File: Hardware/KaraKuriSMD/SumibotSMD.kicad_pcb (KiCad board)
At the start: 2 copper layers, 66 x 51.7 mm, 102 parts, among them J1 USB_B_Micro, M1 Left, M2 Right, Q1 DMG2301L, Q2 DMG2301L, Q3 DMG2301L, Q4 MBT3904DW1, Q5 DMG3406L, SW1 SW_SPDT, SW2 Reset, SW3 Boot, SW4 A, SW5 B, SW6 C, U1 MCP73831-3-OT, U2 AP2112K-3.3, U3 ESP32-WROOM-32, U4 MPU-9250, U5 LP2985-3.3, U6 DRV8870DDA, U7 CH340C, U8 DRV8870DDA

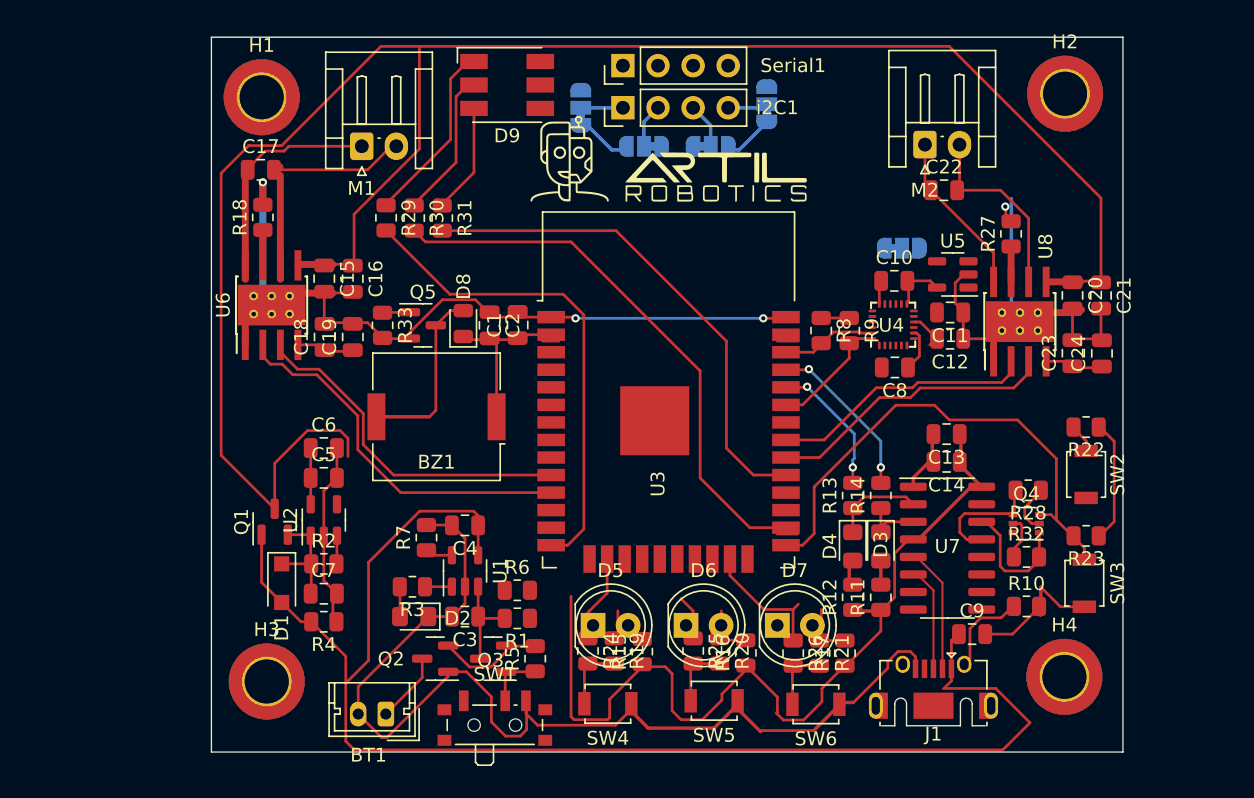
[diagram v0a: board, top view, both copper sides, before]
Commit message: Aplique  jerarquía para trabajar en colaborativo
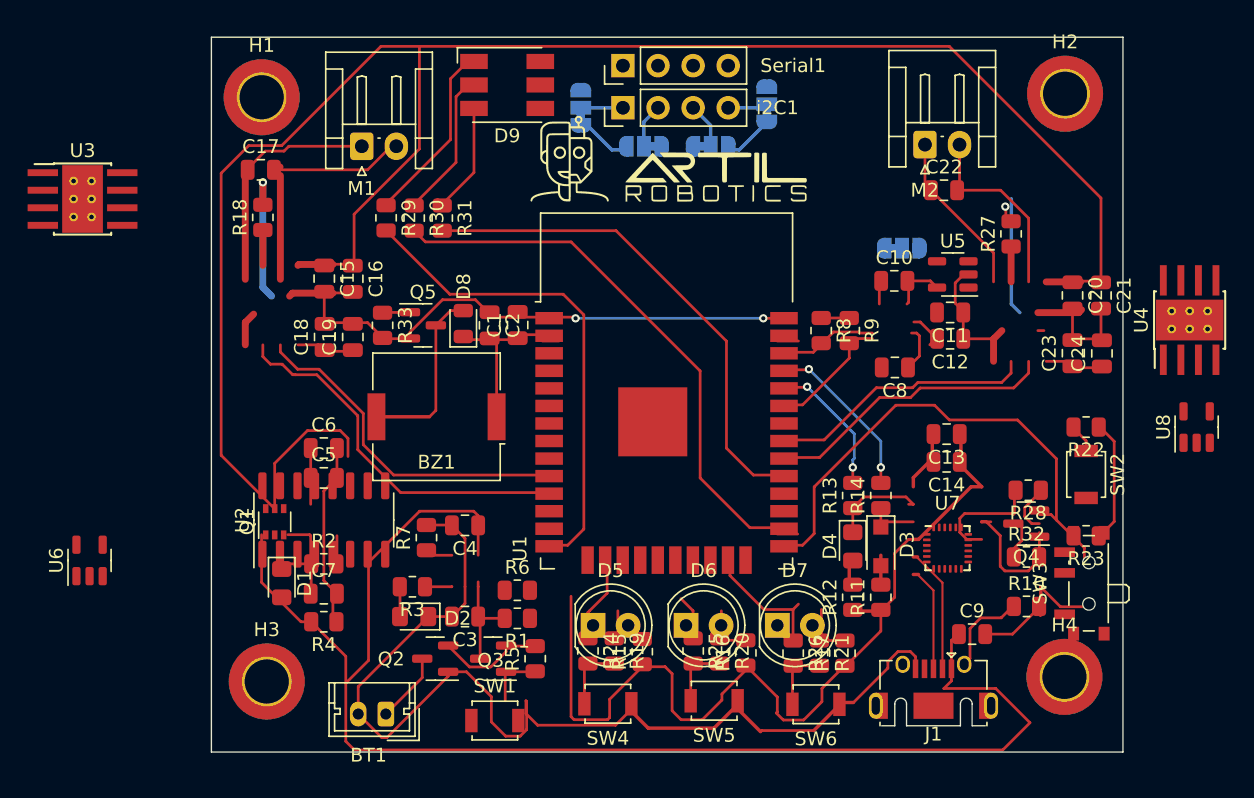
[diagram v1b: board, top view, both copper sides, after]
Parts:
- C10, C15, C20: value 0.1uF -> 10uF
- C11: value 2.2nF -> 0.1uF
- C12: value 0.1uF -> 47uF
- C13, C8: value 10uF -> 3.3nF
- C14: value 10nF -> 0.1uF
- C16, C21: value 47uF -> 10uF
- C17: value 3.3nF -> 10uF
- C18: value 0.1uF -> 1uF
- C22: value 3.3nF -> 0.1uF
- C23: value 0.1uF -> 2.2nF
- C24, C6, C9: value 10uF -> 0.1uF
- C5: value 1uF -> 10nF
- C7: value 10uF -> 47uF
- D1: value MBR1020VL -> LED; footprint Diode_SMD:D_SOD-123F -> LED_SMD:LED_0805_2012Metric_Pad1.15x1.40mm_HandSolder
- D2: value Done -> LED
- D3: value LED -> MBR1020VL; footprint LED_SMD:LED_0805_2012Metric_Pad1.15x1.40mm_HandSolder -> Diode_SMD:D_SOD-123F
- D4: value LED -> Done
- Q1: value DMG2301L -> MBT3904DW1; footprint Package_TO_SOT_SMD:SOT-23 -> Package_TO_SOT_SMD:SOT-363_SC-70-6
- Q4: value MBT3904DW1 -> DMG2301L; footprint Package_TO_SOT_SMD:SOT-363_SC-70-6 -> Package_TO_SOT_SMD:SOT-23
- R1: value 2M -> 10K
- R10: value 0 -> 0.2
- R11: value 1K -> 0.2
- R12: value 1K -> 2M
- R13: value 100 -> 10K
- R14: value 100 -> 1K
- R15: value 1.5K -> 100K
- R16: value 1.5K -> 1M
- R17: value 2.21K -> 2K
- R18: value 0.2 -> 100K
- R22: value 10K -> 1.5K
- R23: value 10K -> 2.21K
- R24, R25: value 3K -> 1K
- R26: value 3K -> 1.5K
- R27: value 0.2 -> 3K
- R28, R29: value 1K -> 3K
- R4: value 100K -> 0
- R5: value 100K -> 1K
- R6: value 1M -> 1K
- R7: value 2K -> 1K
- R8, R9: value 1K -> 100
- SW1: value SW_SPDT -> Reset; footprint Button_Switch_SMD:SW_SPDT_PCM12 -> Button_Switch_SMD:SW_SPST_B3U-1000P
- SW2: value Reset -> Boot
- SW3: value Boot -> SW_SPDT; footprint Button_Switch_SMD:SW_SPST_B3U-1000P -> Button_Switch_SMD:SW_SPDT_PCM12
- U1: value MCP73831-3-OT -> ESP32-WROOM-32; footprint Package_TO_SOT_SMD:SOT-23-5 -> RF_Module:ESP32-WROOM-32
- U2: value AP2112K-3.3 -> CH340C; footprint Package_TO_SOT_SMD:SOT-23-5 -> Package_SO:SOIC-16_3.9x9.9mm_P1.27mm
- U3: value ESP32-WROOM-32 -> DRV8870DDA; footprint RF_Module:ESP32-WROOM-32 -> Package_SO:Texas_HTSOP-8-1EP_3.9x4.9mm_P1.27mm_EP2.95x4.9mm_Mask2.4x3.1mm_ThermalVias
- U4: value MPU-9250 -> DRV8870DDA; footprint Sensor_Motion:InvenSense_QFN-24_3x3mm_P0.4mm -> Package_SO:Texas_HTSOP-8-1EP_3.9x4.9mm_P1.27mm_EP2.95x4.9mm_Mask2.4x3.1mm_ThermalVias
- U5: value LP2985-3.3 -> MCP73831-3-OT
- U6: value DRV8870DDA -> AP2112K-3.3; footprint Package_SO:Texas_HTSOP-8-1EP_3.9x4.9mm_P1.27mm_EP2.95x4.9mm_Mask2.4x3.1mm_ThermalVias -> Package_TO_SOT_SMD:SOT-23-5
- U7: value CH340C -> MPU-9250; footprint Package_SO:SOIC-16_3.9x9.9mm_P1.27mm -> Sensor_Motion:InvenSense_QFN-24_3x3mm_P0.4mm
- U8: value DRV8870DDA -> LP2985-3.3; footprint Package_SO:Texas_HTSOP-8-1EP_3.9x4.9mm_P1.27mm_EP2.95x4.9mm_Mask2.4x3.1mm_ThermalVias -> Package_TO_SOT_SMD:SOT-23-5
- moved U3 45.6 mm to (63.1, 112.0)
- moved U6 22.7 mm to (63.6, 138.2)
- moved U4 21.5 mm to (143.3, 120.8)
- moved U1 17.7 mm to (105.4, 128.9), turned to 0 degrees
- moved U8 14.9 mm to (143.8, 128.5)
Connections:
- C10 pad 1: GND -> +3V8
- C10 pad 2: +3V3 -> GND
- C11 pad 1: GND -> +BATT
- C11 pad 2: unconnected-(C11-Pad2) -> GND
- C12 pad 1: GND -> +BATT
- C12 pad 2: Net-(C12-Pad2) -> GND
- C13 pad 1: +3V3 -> /Motors/B02
- C13 pad 2: GND -> /Motors/B01
- C14 pad 1: +3V3 -> +3V8
- C15 pad 1: +BATT -> +3V8
- C17 pad 1: /A02 -> VBUS
- C17 pad 2: /A01 -> GND
- C18 pad 1: +3V8 -> +3V3
- C19 pad 1: +3V8 -> +3V3
- C20 pad 1: +BATT -> Net-(C20-Pad1)
- C21 pad 1: +BATT -> Net-(C21-Pad1)
- C22 pad 1: /B02 -> GND
- C22 pad 2: /B01 -> +3V3
- C23 pad 1: +3V8 -> GND
- C23 pad 2: GND -> unconnected-(C23-Pad2)
- C24 pad 1: +3V8 -> GND
- C24 pad 2: GND -> Net-(C24-Pad2)
- C3 pad 1: +BATT -> VBUS
- C4 pad 1: VBUS -> +3V3
- C6 pad 1: +3V3 -> +BATT
- C7 pad 1: Net-(C7-Pad1) -> +BATT
- C8 pad 1: Net-(C8-Pad1) -> /Motors/A02
- C8 pad 2: GND -> /Motors/A01
- C9 pad 1: VBUS -> +3V8
- D1 pad 1: Net-(C7-Pad1) -> Net-(D1-Pad1)
- D1 pad 2: VBUS -> Net-(D1-Pad2)
- D2 pad 1: GND -> Net-(D2-Pad1)
- D3 pad 1: Net-(D3-Pad1) -> Net-(C20-Pad1)
- D3 pad 2: Net-(D3-Pad2) -> VBUS
- D4 pad 1: Net-(D4-Pad1) -> GND
- D5 pad 1: /IO1 -> /Sensors/IO1
- D6 pad 1: /IO2 -> /Sensors/IO2
- D7 pad 1: /IO3 -> /Sensors/IO3
- J1 pad 2: /D+ -> /Brain/D+
- J1 pad 3: /D- -> /Brain/D-
- JP3 pad 1: GND -> /Brain/SCL
- JP3 pad 3: +3V3 -> /Brain/SDA
- JP4 pad 1: /SCL -> /Brain/SDA
- JP4 pad 3: /SDA -> /Brain/SCL
- JP5 pad 1: /SDA -> GND
- JP5 pad 3: /SCL -> +3V3
- M1 pad 1: /A02 -> /Motors/A02
- M1 pad 2: /A01 -> /Motors/A01
- M2 pad 1: /B02 -> /Motors/B02
- M2 pad 2: /B01 -> /Motors/B01
- Q1 pad 1: VBUS -> RTS
- Q1 pad 2: Net-(C7-Pad1) -> Net-(Q1-Pad2)
- Q1 pad 3: +BATT -> Boot
- Q2 pad 1: GND -> VBUS
- Q2 pad 2: Net-(Q2-Pad2) -> Net-(C20-Pad1)
- Q2 pad 3: +9V -> +BATT
- Q3 pad 1: Net-(Q3-Pad1) -> GND
- Q3 pad 2: Net-(Q2-Pad2) -> Net-(Q3-Pad2)
- Q3 pad 3: +BATT -> +9V
- Q4 pad 1: RTS -> Net-(Q4-Pad1)
- Q4 pad 2: Net-(Q4-Pad2) -> Net-(Q3-Pad2)
- Q4 pad 3: Boot -> +BATT
- Q5 pad 1: /Buzzer -> /OutPuts/Buzzer
- R1 pad 1: /BM -> +3V3
- R1 pad 2: +BATT -> /Brain/Reset
- R10 pad 1: Net-(J1-Pad6) -> Net-(R10-Pad1)
- R11 pad 1: +3V3 -> Net-(R11-Pad1)
- R11 pad 2: Net-(D3-Pad2) -> GND
- R12 pad 1: +3V3 -> /Brain/BattMeter
- R12 pad 2: Net-(D4-Pad2) -> +BATT
- R13 pad 1: Net-(D4-Pad1) -> Net-(C20-Pad1)
- R13 pad 2: TXD -> Net-(R13-Pad2)
- R14 pad 1: Net-(D3-Pad1) -> Net-(R14-Pad1)
- R14 pad 2: RXD -> Net-(D4-Pad2)
- R15 pad 1: +3V3 -> GND
- R15 pad 2: Net-(D5-Pad2) -> VBUS
- R16 pad 1: +3V3 -> GND
- R16 pad 2: Net-(D6-Pad2) -> /Brain/BattMeter
- R17 pad 1: +3V3 -> Net-(R17-Pad1)
- R17 pad 2: Net-(D7-Pad2) -> GND
- R18 pad 1: Net-(R18-Pad1) -> Net-(Q4-Pad1)
- R18 pad 2: GND -> Net-(Q3-Pad2)
- R19 pad 1: Net-(D5-Pad2) -> +3V3
- R19 pad 2: Net-(R19-Pad2) -> /Sensors/SCL
- R2 pad 1: Net-(C7-Pad1) -> +3V3
- R2 pad 2: Net-(R2-Pad2) -> Boot
- R20 pad 1: Net-(D6-Pad2) -> +3V3
- R20 pad 2: Net-(R20-Pad2) -> /Sensors/SDA
- R21 pad 1: Net-(D7-Pad2) -> +3V3
- R21 pad 2: Net-(R21-Pad2) -> Net-(D5-Pad2)
- R22 pad 2: /Reset -> Net-(D6-Pad2)
- R23 pad 2: Boot -> Net-(D7-Pad2)
- R24 pad 1: /IO1 -> Net-(D5-Pad2)
- R24 pad 2: Net-(R19-Pad2) -> Net-(R24-Pad2)
- R25 pad 1: /IO2 -> Net-(D6-Pad2)
- R25 pad 2: Net-(R20-Pad2) -> Net-(R25-Pad2)
- R26 pad 1: /IO3 -> Net-(D7-Pad2)
- R26 pad 2: Net-(R21-Pad2) -> Net-(R26-Pad2)
- R27 pad 1: Net-(R27-Pad1) -> /Sensors/IO1
- R27 pad 2: GND -> Net-(R24-Pad2)
- R28 pad 1: Net-(Q4-Pad2) -> /Sensors/IO2
- R28 pad 2: DTR -> Net-(R25-Pad2)
- R29 pad 1: Net-(D9-Pad1) -> /Sensors/IO3
- R29 pad 2: /R_led -> Net-(R26-Pad2)
- R3 pad 1: Net-(R3-Pad1) -> Net-(Q1-Pad2)
- R3 pad 2: Net-(D2-Pad2) -> DTR
- R30 pad 1: Net-(D9-Pad2) -> Net-(D9-Pad1)
- R30 pad 2: /G_led -> /OutPuts/R_led
- R31 pad 1: Net-(D9-Pad3) -> Net-(D9-Pad2)
- R31 pad 2: /B_led -> /OutPuts/G_led
- R32 pad 1: Net-(Q4-Pad5) -> Net-(D9-Pad3)
- R32 pad 2: RTS -> /OutPuts/B_led
- R33 pad 1: /Buzzer -> /OutPuts/Buzzer
- R4 pad 1: GND -> Net-(J1-Pad6)
- R4 pad 2: VBUS -> GND
- R5 pad 1: Net-(Q3-Pad1) -> Net-(Q1-Pad5)
- R5 pad 2: Net-(Q2-Pad2) -> RTS
- R6 pad 1: GND -> +3V3
- R6 pad 2: /BM -> Net-(D1-Pad2)
- R7 pad 1: Net-(R7-Pad1) -> +3V3
- R7 pad 2: GND -> Net-(D2-Pad2)
- R8 pad 1: +3V3 -> Net-(D2-Pad1)
- R8 pad 2: /SCL -> TXD
- R9 pad 1: +3V3 -> Net-(D1-Pad1)
- R9 pad 2: /SDA -> RXD
- SW1 pad 1: unconnected-(SW1-Pad1) -> GND
- SW1 pad 2: Net-(Q3-Pad1) -> /Brain/Reset
- SW2 pad 2: /Reset -> Boot
- SW3 pad 1: GND -> unconnected-(SW3-Pad1)
- SW3 pad 2: Boot -> Net-(Q4-Pad1)
- SW4 pad 2: Net-(R19-Pad2) -> Net-(R24-Pad2)
- SW5 pad 2: Net-(R20-Pad2) -> Net-(R25-Pad2)
- SW6 pad 2: Net-(R21-Pad2) -> Net-(R26-Pad2)
- U1 pad 1: Net-(R3-Pad1) -> GND
- U1 pad 2: GND -> +3V3
- U1 pad 3: +BATT -> EN
- U1 pad 4: VBUS -> unconnected-(U1-Pad4)
- U1 pad 5: Net-(R7-Pad1) -> unconnected-(U1-Pad5)
- U2 pad 1: Net-(C7-Pad1) -> GND
- U2 pad 2: GND -> Net-(D2-Pad1)
- U2 pad 3: Net-(R2-Pad2) -> Net-(D1-Pad1)
- U2 pad 4: unconnected-(U2-Pad4) -> +3V3
- U2 pad 5: +3V3 -> /Brain/D+
- U3 pad 2: +3V3 -> /Brain/PWM_IN2A
- U3 pad 3: EN -> /Brain/PWM_IN1A
- U3 pad 4: unconnected-(U3-Pad4) -> +3V8
- U3 pad 5: unconnected-(U3-Pad5) -> +BATT
- U3 pad 6: unconnected-(U3-Pad6) -> /Motors/A01
- U3 pad 7: /BM -> Net-(R10-Pad1)
- U3 pad 8: unconnected-(U3-Pad8) -> /Motors/A02
- U3 pad 9: unconnected-(U3-Pad9) -> GND
- U4 pad 1: unconnected-(U4-Pad1) -> GND
- U4 pad 2: (no net) -> /Brain/PWM_IN2B
- U4 pad 3: (no net) -> /Brain/PWM_IN1B
- U4 pad 4: (no net) -> +3V8
- U4 pad 5: (no net) -> +BATT
- U4 pad 6: (no net) -> /Motors/B01
- U4 pad 7: unconnected-(U4-Pad7) -> Net-(R11-Pad1)
- U4 pad 8: Net-(C8-Pad1) -> /Motors/B02
- U4 pad 9: Net-(JP2-Pad2) -> GND
- U5 pad 1: VBUS -> Net-(R14-Pad1)
- U5 pad 3: unconnected-(U5-Pad3) -> +BATT
- U5 pad 4: unconnected-(U5-Pad4) -> VBUS
- U5 pad 5: +3V3 -> Net-(R17-Pad1)
- U6 pad 1: GND -> Net-(C20-Pad1)
- U6 pad 2: /PWM_IN2A -> GND
- U6 pad 3: /PWM_IN1A -> Net-(R13-Pad2)
- U6 pad 4: +3V8 -> unconnected-(U6-Pad4)
- U6 pad 5: +BATT -> +3V3
- U7 pad 1: GND -> unconnected-(U7-Pad1)
- U7 pad 10: unconnected-(U7-Pad10) -> Net-(C24-Pad2)
- U7 pad 13: DTR -> +3V3
- U7 pad 14: RTS -> (no net)
- U7 pad 15: unconnected-(U7-Pad15) -> (no net)
- U7 pad 16: +3V3 -> (no net)
- U7 pad 2: Net-(D4-Pad1) -> (no net)
- U7 pad 3: Net-(D3-Pad1) -> (no net)
- U7 pad 4: +3V3 -> (no net)
- U7 pad 5: /D+ -> (no net)
- U7 pad 6: /D- -> (no net)
- U7 pad 8: unconnected-(U7-Pad8) -> Net-(C21-Pad1)
- U7 pad 9: unconnected-(U7-Pad9) -> Net-(JP5-Pad2)
- U8 pad 1: GND -> VBUS
- U8 pad 2: /PWM_IN2B -> GND
- U8 pad 3: /PWM_IN1B -> unconnected-(U8-Pad3)
- U8 pad 4: +3V8 -> unconnected-(U8-Pad4)
- U8 pad 5: +BATT -> +3V3
- i2C1 pad 2: Net-(JP3-Pad2) -> Net-(JP2-Pad2)
- i2C1 pad 3: Net-(JP4-Pad2) -> Net-(JP3-Pad2)
- i2C1 pad 4: Net-(JP5-Pad2) -> Net-(JP4-Pad2)
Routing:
- net GND: track 194.6 -> 392.6 mm, vias 4 -> 2
- net Net-(BZ1-Pad2): track 13.1 -> 155.2 mm
- net +BATT: track 149.7 -> 18.8 mm
- net VBUS: track 102.0 -> 2.04 mm
- net +3V3: track 102.8 -> 40.1 mm
- net Net-(D7-Pad2): track 4.39 -> 50.9 mm
- net /OutPuts/R_led: track 0.00 -> 40.4 mm
- net /G_led: track 41.8 -> 1.48 mm
- net Net-(R26-Pad2): track 0.00 -> 40.2 mm
- net /OutPuts/G_led: track 0.00 -> 36.7 mm
- net /B_led: track 36.7 -> 0.00 mm
- net /R_led: track 35.2 -> 0.00 mm
- net Boot: track 36.9 -> 4.20 mm
- net /PWM_IN2A: track 27.2 -> 0.00 mm
- net /Brain/PWM_IN2A: track 0.00 -> 27.2 mm
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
